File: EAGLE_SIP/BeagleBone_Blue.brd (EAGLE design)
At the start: 86.4 x 54.6 mm, 202 parts, among them J1 USD_CONNECTOR, M1 JST_ZH_2, M2 JST_ZH_2, M3 JST_ZH_2, M4 JST_ZH_2, Q3 MOSFET-N, U5 24LC_32AT-I/OT, U6 SN74LVC1G07_DCK_5, Y1 CM200C-32.768KAZF-UT, Y2 445C33D24M00000

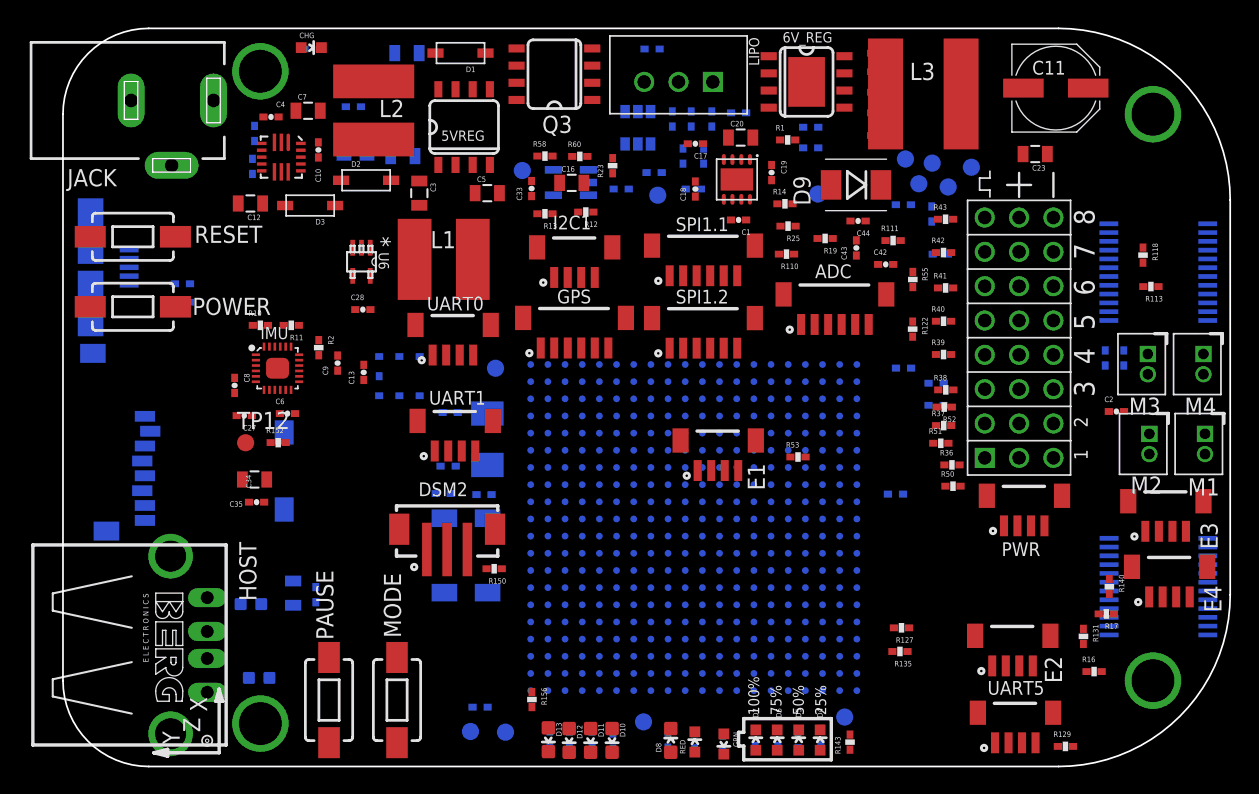
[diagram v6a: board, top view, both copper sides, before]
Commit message: Switch to Sunstone DRU
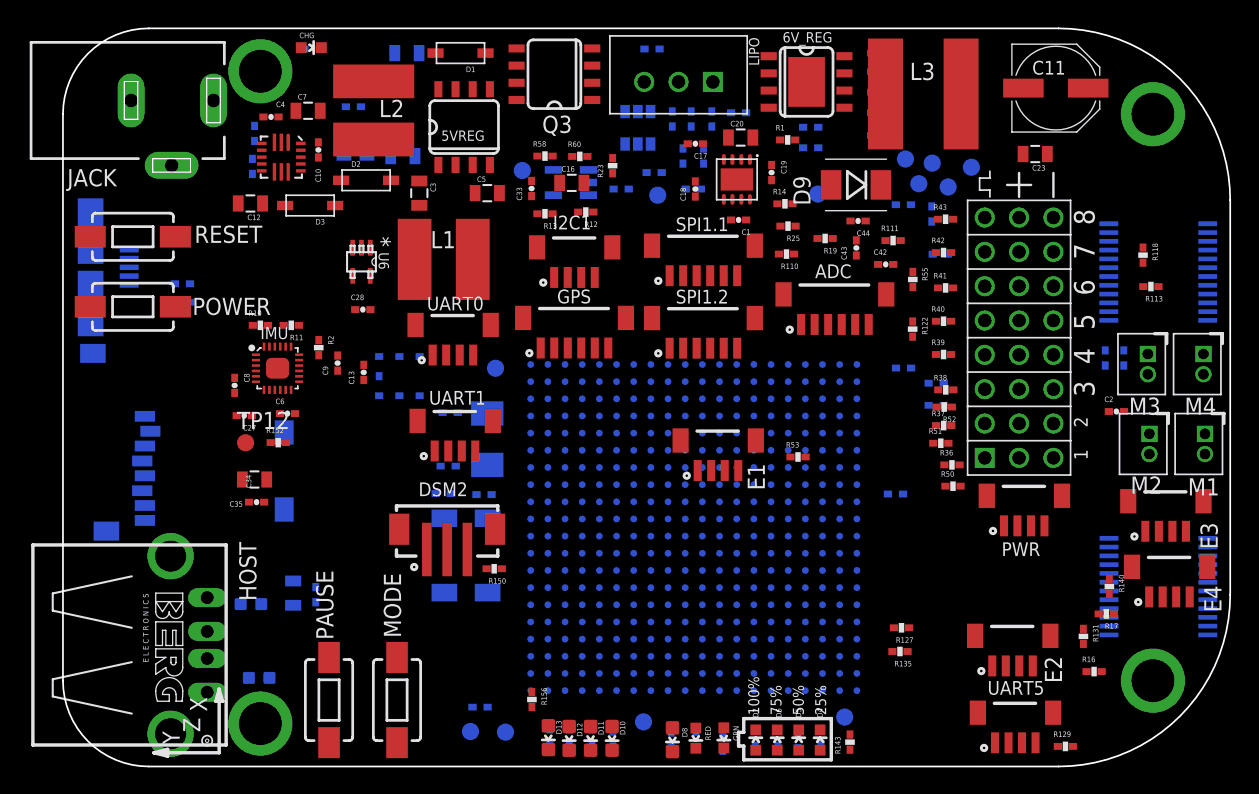
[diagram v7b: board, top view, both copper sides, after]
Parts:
- moved GRN 0.46 mm to (48.9, -52.5)
- moved RED 0.29 mm to (46.8, -52.5), turned to 180 degrees
- moved R24 0.25 mm to (45.0, -52.7), turned to 90 degrees
- moved D10 0.15 mm to (40.6, -52.5)
- moved D11 0.15 mm to (39.0, -52.5)
- moved D12 0.15 mm to (37.5, -52.5)
- moved D13 0.15 mm to (35.9, -52.5)
- moved R61 0.15 mm to (40.7, -52.6)
- moved R62 0.15 mm to (39.1, -52.4)
- moved R63 0.15 mm to (37.5, -52.4)
- moved R64 0.15 mm to (36.0, -52.4)
- moved R21 0.14 mm to (46.8, -52.6), turned to 90 degrees
- moved D8 0.14 mm to (45.1, -52.6), turned to 180 degrees

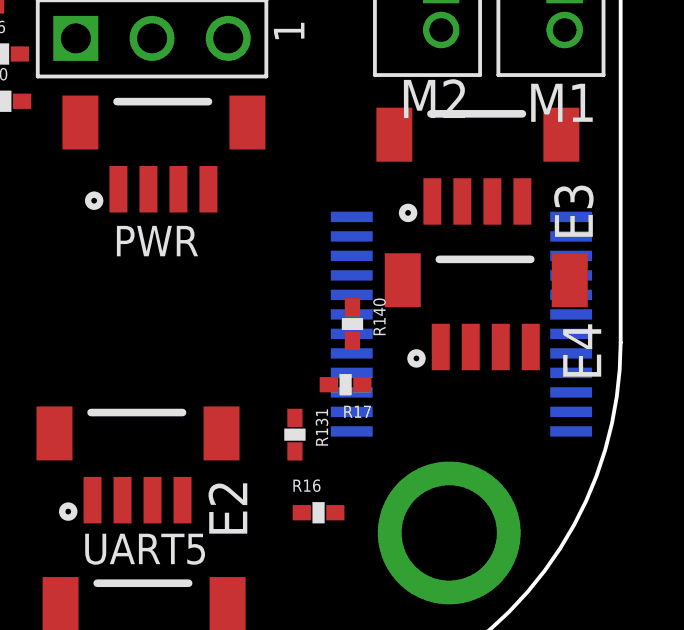
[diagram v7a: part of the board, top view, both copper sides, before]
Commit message: DRC fix
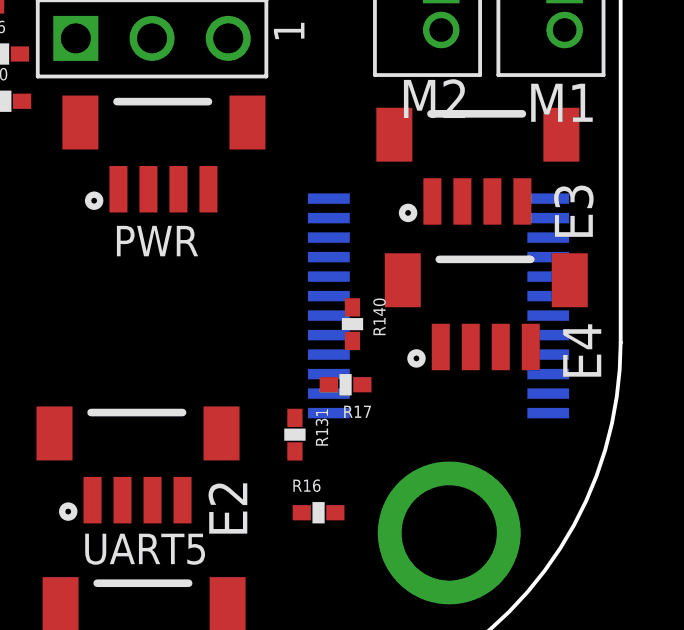
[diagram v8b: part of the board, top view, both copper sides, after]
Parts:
- moved H1 0.98 mm to (80.3, -40.7)
